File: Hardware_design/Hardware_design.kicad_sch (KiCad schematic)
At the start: 21 parts, among them SW1 SW_Push, U1 STM32L073RZT6, Y1 32.768Khz, Y2 8Mhz

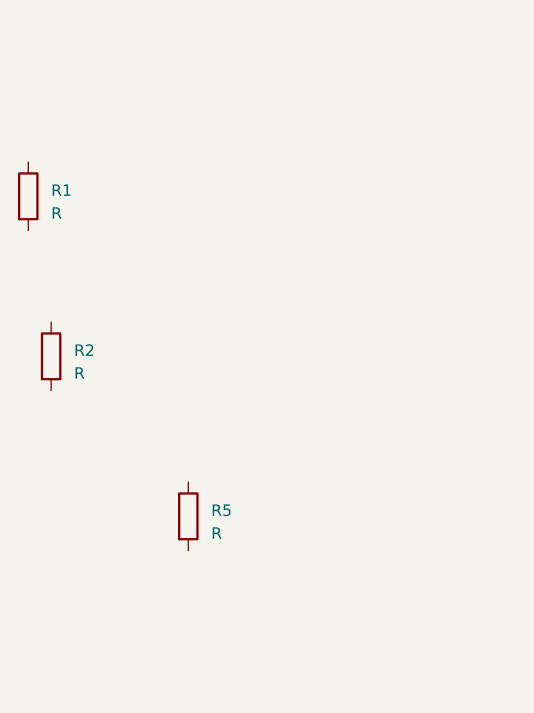
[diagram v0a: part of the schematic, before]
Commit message: Deleted extra components
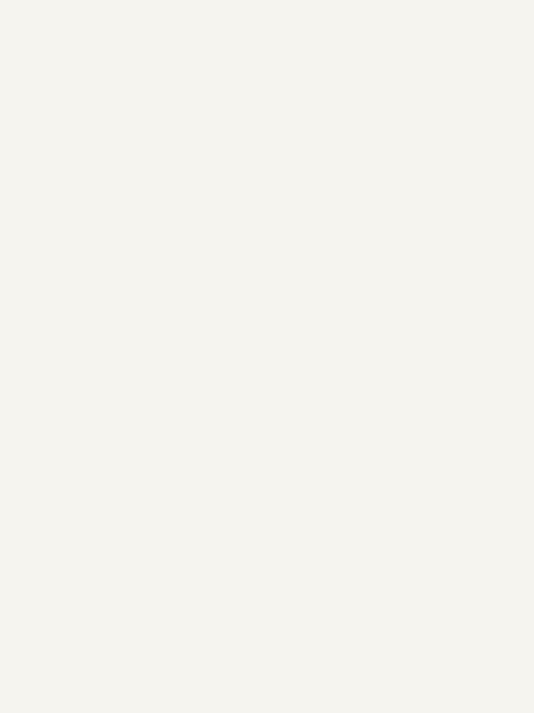
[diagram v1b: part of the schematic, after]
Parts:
- removed R1, R2, R5: R, symbol Device:R
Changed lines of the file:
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@@
-    )
-  )
-  (symbol (lib_id "Device:R") (at -41.91 69.85 0) (unit 1)
-    (in_bom yes) (on_board yes) (dnp no) (fields_autoplaced)
-    (property "Reference" "R1" (at -39.37 69.215 0)
-      (effects (font (size 1.27 1.27)) (justify left))
-    )
-    (property "Value" "R" (at -39.37 71.755 0)
-      (effects (font (size 1.27 1.27)) (justify left))
-    )
-    (property "Footprint" "" (at -43.688 69.85 90)
-      (effects (font (size 1.27 1.27)) hide)
-    )
-    (property "Datasheet" "~" (at -41.91 69.85 0)
-      (effects (font (size 1.27 1.27)) hide)
-    )
-    (pin "1")
-    (pin "2")
-    (instances
-      (project "Hardware_design"
-        (path "/4f9f9259-5af2-41ae-a3f8-1f750e6c5dae"
-          (reference "R1") (unit 1)
-        )
-      )
     )
   )
@@
         (path "/4f9f9259-5af2-41ae-a3f8-1f750e6c5dae"
           (reference "C7") (unit 1)
-        )
-      )
-    )
-  )
-  (symbol (lib_id "Device:R") (at -39.37 87.63 0) (unit 1)
-    (in_bom yes) (on_board yes) (dnp no) (fields_autoplaced)
-    (property "Reference" "R2" (at -36.83 86.995 0)
-      (effects (font (size 1.27 1.27)) (justify left))
-    )
-    (property "Value" "R" (at -36.83 89.535 0)
-      (effects (font (size 1.27 1.27)) (justify left))
-    )
-    (property "Footprint" "" (at -41.148 87.63 90)
-      (effects (font (size 1.27 1.27)) hide)
-    )
-    (property "Datasheet" "~" (at -39.37 87.63 0)
-      (effects (font (size 1.27 1.27)) hide)
-    )
-    (pin "1")
-    (pin "2")
-    (instances
-      (project "Hardware_design"
-        (path "/4f9f9259-5af2-41ae-a3f8-1f750e6c5dae"
-          (reference "R2") (unit 1)
         )
       )
@@
         )
       )
-    )
-  )
-  (symbol (lib_id "Device:R") (at -24.13 105.41 0) (unit 1)
-    (in_bom yes) (on_board yes) (dnp no) (fields_autoplaced)
-    (property "Reference" "R5" (at -21.59 104.775 0)
-      (effects (font (size 1.27 1.27)) (justify left))
-    )
-    (property "Value" "R" (at -21.59 107.315 0)
-      (effects (font (size 1.27 1.27)) (justify left))
-    )
-    (property "Footprint" "" (at -25.908 105.41 90)
-      (effects (font (size 1.27 1.27)) hide)
-    )
-    (property "Datasheet" "~" (at -24.13 105.41 0)
-      (effects (font (size 1.27 1.27)) hide)
-    )
-    (pin "1")
-    (pin "2")
-    (instances
-      (project "Hardware_design"
-        (path "/4f9f9259-5af2-41ae-a3f8-1f750e6c5dae"
-          (reference "R5") (unit 1)
-        )
-      )

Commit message: LTE,LDOs,and battery charging circuit are added
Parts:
- removed C6: 1uF, symbol Device:C
- added 02x04_Connector1: ~, symbol 2x04_Connector:2x04_Connector
- added C1, C2: 100nF, symbol Device:C
- added C11, C28, C36, C41, C43: 0.1uf, symbol Device:C
- added C14, C17: 0.1uF, symbol Device:C
- added C15, C16: 10uF, symbol Device:C
- added C18, C23: 0.1uF, Capacitor_SMD:C_0603_1608Metric, symbol Device:C
- added C19: 10uF, Capacitor_SMD:C_0603_1608Metric, symbol Device:C
- added C20, C25, C26: 100uF, Capacitor_SMD:C_0603_1608Metric, symbol Device:C
- added C21: 100nF, Capacitor_SMD:C_0603_1608Metric, symbol Device:C
- added C22: 220pF, Capacitor_SMD:C_0603_1608Metric, symbol Device:C
- added C24: 22uF, Capacitor_SMD:C_0603_1608Metric, symbol Device:C
- added C27, C38, C48: 1uf, symbol Device:C
- added C29, C30, C31, C32, C33, C34, C37, C40: 22uf, symbol Device:C
- added C35: C, symbol Device:C
- added C39, C42, C44, C45, C46, C47: 100uf, symbol Device:C
- added C49, C50: 33pf, symbol Device:C
- added C51, C52, C53: 100nf, symbol Device:C
- added D1: LED_RGB, symbol Device:LED_RGB
- added D2: SS34, Diode_SMD:D_SMC, symbol Device:D_Schottky
- added D3: LED, LED_SMD:LED_0805_2012Metric, symbol Device:LED
- added J1: USB_C_Receptacle_PowerOnly_6P, symbol Connector:USB_C_Receptacle_PowerOnly_6P
- added J3: USB_B_Micro, symbol Connector:USB_B_Micro
- added L1: 10uH, Inductor_SMD:L_Bourns-SRN6028, symbol Device:L
- added L2: 2.2uH, symbol Device:L
- added PS1: LD39200DPUR, SON80P400X400X100-9N-D, symbol LDO:LD39200DPUR
- added Q1, Q2, Q3: MMUN2233LT1G, SOT96P237X111-3N, symbol MMUN2233LT1G:MMUN2233LT1G
- added R1, R2, R3: 1K, symbol Device:R
- added R10: 68.1K, Resistor_SMD:R_0805_2012Metric, symbol Device:R
- added R11, R8: 124K, Resistor_SMD:R_0805_2012Metric, symbol Device:R
- added R12: 100K, Resistor_SMD:R_0805_2012Metric, symbol Device:R
- added R13: 1K, Resistor_SMD:R_0805_2012Metric, symbol Device:R
- added R14: 31.6k, symbol Device:R
- added R15, R17, R21, R22, R28, R29, R32: 10k, symbol Device:R
- added R16, R34, R35, R36, R37: 0R, symbol Device:R
- added R18: 13.3k, symbol Device:R
- added R19: 40k, symbol Device:R
- added R20: 37.4k, symbol Device:R
- added R23: 23.7k, symbol Device:R
- added R24, R26: 5.1k, symbol Device:R
- added R25: 15k, symbol Device:R
- added R27: 6.6k, symbol Device:R
- added R30, R33: 6.65k, symbol Device:R
- added R31: 25.5k, symbol Device:R
- added R4, R5: 10K, symbol Device:R
- added R9: 24.9K, Resistor_SMD:R_0805_2012Metric, symbol Device:R
- added SW1, SW2, SW4: SW_Push, symbol Switch:SW_Push
- added U2: TLV70333DBVR, symbol LDO:TLV70333DBVR
- added U3: MP1584EN-LF-Z, footprints:SOIC8E_MPS, symbol 2024-05-29_15-09-36:MP1584EN-LF-Z
- added U4: MP2636GR-P, QFN-4x4_MP2636_MNP, symbol MP2636:MP2636GR-P
- added U5: SIM7600E-H, SIM7600E-H:IC_SIM7600E-H, symbol SIM7600E-H:SIM7600E-H
- added U6: TXB0104RGY, Package_DFN_QFN:Texas_S-PVQFN-N14, symbol Logic_LevelTranslator:TXB0104RGY
- added U7: USBLC6-2SC6, Package_TO_SOT_SMD:SOT-23-6, symbol Power_Protection:USBLC6-2SC6
- renumbered C9 to C10, C2 to C12, C8 to C13, C7 to C3, C5 to C4, C11 to C5, C10 to C6, C3 to C7, C4 to C8, C1 to C9, R3 to R6, R4 to R7, SW1 to SW3, Y2 to Y1, Y1 to Y2
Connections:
- net +3V3: now also C16.1, C17.1, R4.2, R5.2, U2.5 (OUT)
- net DBG_UART_RX: now also 02x04_Connector1.6
- net DBG_UART_TX: now also 02x04_Connector1.5
- net GND: now also C1.2, C11.2, C14.2, C15.2, C16.2, C17.2, C18.2, C19.2, C2.2, C20.2, C23.2, C24.2, C25.2, C26.2, C27.1, C28.1, C29.1, C30.1, C31.1, C32.1, C33.2, C34.2, C37.2, C38.2, C39.2, C40.2, C41.2, C42.2, C43.1, C44.1, C45.1, C46.1, C47.1, C48.1, C49.1, C50.1, C51.2, C52.1, C53.2, D1.1 (RK), D1.2 (GK), D1.3 (BK), D2.2 (A), D3.1 (K), J1.A12 (GND), J1.B12 (GND), J1.S1 (SHIELD), J3.5 (GND), J3.6 (Shield), PS1.4 (GND_1), PS1.9 (GND_2), Q1.2 (E), Q2.2 (E), Q3.2 (E), R10.2, R12.2, R16.2, R28.2, R9.2, SW1.1, SW2.1, SW4.2, U2.2 (GND), U3. (EPAD), U3.5 (GND), U4.28 (PGND), U5.1 (GND), U5.10 (GND), U5.14 (GND), U5.2 (GND), U5.37 (GND), U5.40 (GND), U5.41 (GND), U5.43 (GND), U5.5 (GND), U5.57 (GND), U5.58 (GND), U5.60 (GND), U5.61 (GND), U5.64 (GND), U5.65 (GND), U5.77 (GND), U5.78 (GND), U5.80 (GND), U5.81 (GND), U6.15 (Pad), U6.7 (GND), U7.2 (GND)
- net GNDA: now also C35.2, C36.2, R15.1, R16.1, R18.1, R19.1, R20.1, R24.2, R26.2, R31.1, U4.15 (AGND), U4.26 (FREQ)
- net LED_1: now also R1.2
- net LED_2: now also R2.2
- net LED_3: now also R3.2
- net MCU_TO_MODEM_UART_RX: now also U6.10 (B4)
- net MCU_TO_MODEM_UART_TX: now also U6.13 (B1)
- net SWCLK: now also 02x04_Connector1.4
- net SWDIO: now also 02x04_Connector1.1
- net SW1: now reaches U1.57 (PB5)
- net SW1: now also C1.1, R4.1, SW1.2
- net SW2: now reaches U1.58 (PB6)
- net SW2: now also C2.1, R5.1, SW2.2
- net LTEMODEM_ON_OFF renamed LTEMODEM_ONOFF
- net LTEMODEM_ONOFF: now also Q1.1 (B)
- net LTE_MODEM_LDO renamed LDO_LTEMODEM_EN
- net LDO_LTEMODEM_EN: now also Q2.1 (B)
- net LTE_MODEM_RST renamed LTEMODEM_RESET
- net LTEMODEM_RESET: now also Q3.1 (B)
- new net: R37.2, U6.5 (A4)
- new net: R30.1, R31.2, U4.12 (NTC)
- new net: R17.1, U4.16 (VB)
- new net: C35.1, R17.2, R21.2, R22.2
- new net: PS1.6 (EN), Q2.3 (C), R29.2
- new net: C23.1, C24.1, C25.1, C26.1, L1.2, R11.2, R13.1
- new net: D3.2 (A), R13.2
- new net: C11.1, C37.1, C38.1, J1.A9 (VBUS), J1.B9 (VBUS), R23.1, R25.1, U4.4 (VIN)
- new net: R23.2, R26.1, U4.7 (PWIN)
- new net: R35.2, U6.3 (A2)
- new net: R18.2, U4.6 (ILIM)
- new net: R34.2, U6.2 (A1)
- new net: R36.2, U6.4 (A3)
- new net: C36.1, U4.8 (TMR)
- new net: C27.2, C28.2, C29.2, C30.2, C31.2, C32.2, R14.2, U4.3 (SYS)
- new net: C18.1, C19.1, C20.1, R8.1, U3.7 (VIN)
- new net: R24.1, R25.2, U4.9 (REG)
- new net: PS1.3 (ADJ/SENSE), R27.2, R28.1
- new net: R14.1, R15.2, R32.1
- new net: R32.2, U4.11 (FB)
- new net: R19.2, U4.13 (ISET)
- new net: R20.2, U4.14 (OLIM)
- new net: L2.1, U4.21 (SW)
- new net: R21.1, U4.24 (MODE)
- new net: R22.1, U4.25 (EN)
- new net: C21.1, U3.8 (BST)
- new net: C21.2, D2.1 (K), L1.1, U3.1 (SW)
- new net: D1.5 (GA), R2.1
- new net: R8.2, U3.2 (EN)
- new net: D1.6 (RA), R3.1
- new net: D1.4 (BA), R1.1
- new net: C22.2, R10.1
- new net: 02x04_Connector1.7, 02x04_Connector1.8
- new net: L2.2, R33.1
- new net: R11.1, R12.1, U3.4 (FB)
- new net: C22.1, U3.3 (COMP)
- new net: R9.1, U3.6 (FREQ)
- new net +3.3V: C53.1, U6.14 (VCCB)
- new net +5V: C14.1, C15.1, U2.1 (IN), U2.3 (EN)
- new net 1.8V: C52.2, U6.1 (VCCA), U6.8 (OE)
- new net BATT+: C33.1, C34.1, C40.1, R33.2
- new net BATT_CHAG_OUT: R30.2
- new net MODEM_RX: R36.1, R37.1
- new net MODEM_TX: R34.1, R35.1
- new net NRST: 02x04_Connector1.2
- new net POWERKEY: C51.1, Q1.3 (C), SW4.1, U5.3 (PWRKEY)
- new net RESET: Q3.3 (C), U5.4 (RESET)
- new net USB_N: J3.2 (D-), U5.12 (USB_DN), U7.3 (I/O2), U7.4 (I/O2)
- new net USB_P: J3.3 (D+), U5.13 (USB_DP), U7.1 (I/O1), U7.6 (I/O1)
- new net USB_TO_MODEM_RX: U6.11 (B3)
- new net USB_TO_MODEM_TX: U6.12 (B2)
- new net USB_VBUS: J3.1 (VBUS), U5.11 (USB_VBUS)
- new net VCC_LTE_MODEM: C39.1, C41.1, C42.1, C43.2, C44.2, C45.2, C46.2, C47.2, C48.2, C49.2, C50.2, PS1.1 (OUT_1), PS1.2 (OUT_2), PS1.7 (IN_1), PS1.8 (IN_2), R27.1, R29.1, U5.38 (VBAT), U5.39 (VBAT), U5.62 (VBAT), U5.63 (VBAT)
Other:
- added sheet Battery charging  (Battery_charging_sch.kicad_sch)
- added sheet GSM (GSM.kicad_sch)
- added sheet SMPS (SMPS_sch.kicad_sch)
- note added: "4G_LTE_MODEM"
- note added: "BATTERY_CHARGER_IC"
- note added: "GSM_USB_INTERFACE"
- note added: "LED INDICATION"
- note added: "LTEMODEM_ON_OFF_RESET"
- note added: "LTE_MODEM_LDO"
- note added: "SMPS_AND_LDO"
- note added: "STM32_MCU"
- note added: "STM32_MCU_CIRCUIT"
- note added: "SWD_DEBUG_INTERFACE"
- note added: "SWITCH INPUT"
- moved on the sheet: C10, C12, C13, C3, C4, C5, C6, C7, C8, C9, FB1, R6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
